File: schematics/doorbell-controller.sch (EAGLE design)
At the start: 2 parts

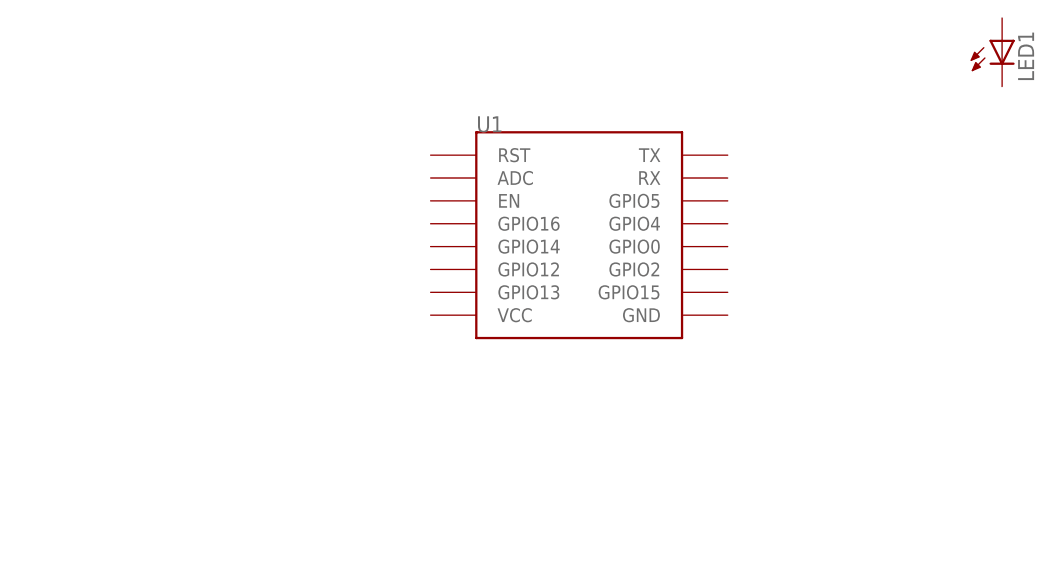
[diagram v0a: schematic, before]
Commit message: Added interrupt extender to schematics
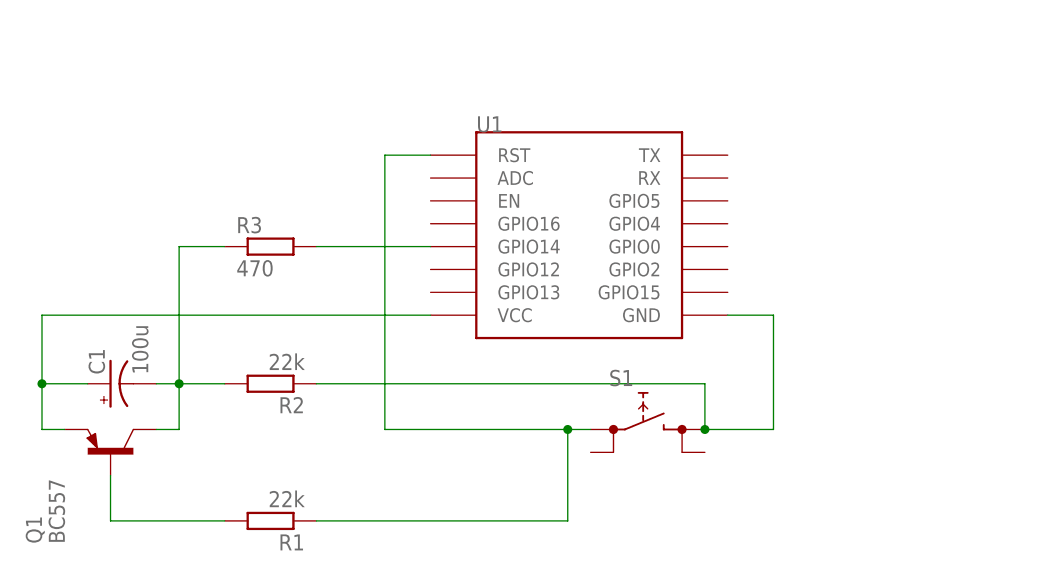
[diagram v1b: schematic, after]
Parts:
- removed LED1: (no value), led:LED5MM
- added C1: 100u, rcl:CPOL-USE2,5-6E
- added Q1: BC557, transistor-pnp:BC557
- added R1, R2: 22k, rcl:R-EU_0204/7
- added R3: 470, rcl:R-EU_0204/7
- added S1: (no value), switch:REKN
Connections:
- new net GND: R2.1, S1.1@A, U1.GND
- new net N$2: Q1.B, R1.2
- new net N$3: R3.2, U1.GPIO14
- new net N$5: C1.-, Q1.C, R2.2, R3.1
- new net N$8: C1.+, Q1.E, U1.VCC
- new net RST: R1.1, S1.0@A, U1.RST

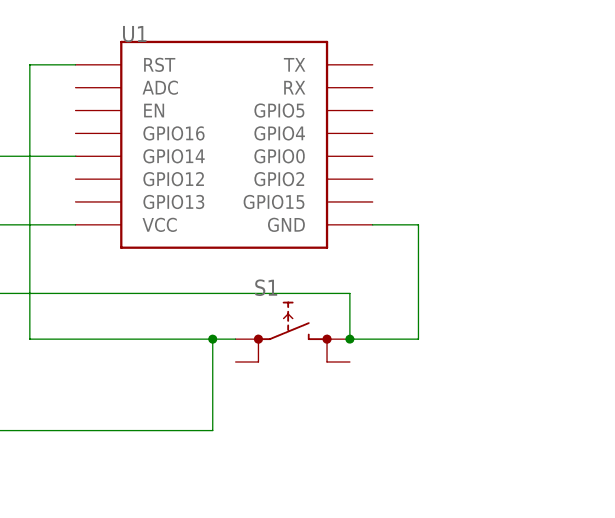
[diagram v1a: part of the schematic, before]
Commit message: Added LEDs to schematics; Replaces button with Clamp
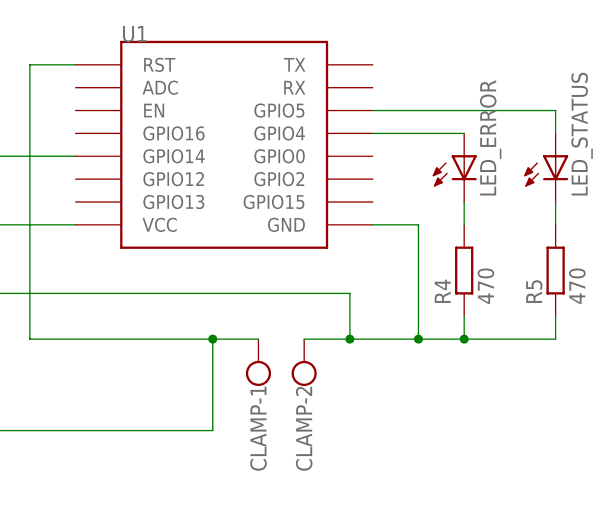
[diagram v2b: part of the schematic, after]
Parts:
- removed S1: (no value), switch:REKN
- added CLAMP: (no value), con-wago-500:W237-102
- added LED_ERROR, LED_STATUS: (no value), led:LED5MM
- added R4, R5: 470, rcl:R-EU_0204/7
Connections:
- new net N$1: LED_STATUS.A, U1.GPIO5
- new net N$4: LED_ERROR.A, U1.GPIO4
- new net N$6: LED_ERROR.C, R4.2
- new net N$7: LED_STATUS.C, R5.2
- net GND: now also CLAMP-2.KL, R4.1, R5.1; no longer S1.1@A
- net RST: now also CLAMP-1.KL; no longer S1.0@A
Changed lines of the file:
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@@
 <part name="R1" library="rcl" library_urn="urn:adsk.eagle:library:334" deviceset="R-EU_" device="0204/7" package3d_urn="urn:adsk.eagle:package:23498/1" value="22k"/>
 <part name="C1" library="rcl" library_urn="urn:adsk.eagle:library:334" deviceset="CPOL-US" device="E2,5-6E" package3d_urn="urn:adsk.eagle:package:23430/1" value="100u"/>
-<part name="S1" library="switch" library_urn="urn:adsk.eagle:library:380" deviceset="REKN" device="" package3d_urn="urn:adsk.eagle:package:27692/1"/>
 <part name="R2" library="rcl" library_urn="urn:adsk.eagle:library:334" deviceset="R-EU_" device="0204/7" package3d_urn="urn:adsk.eagle:package:23498/1" value="22k"/>
 <part name="Q1" library="transistor-pnp" library_urn="urn:adsk.eagle:library:399" deviceset="BC557" device="" package3d_urn="urn:adsk.eagle:package:29211/2"/>
 <part name="R3" library="rcl" library_urn="urn:adsk.eagle:library:334" deviceset="R-EU_" device="0204/7" package3d_urn="urn:adsk.eagle:package:23498/1" value="470"/>
+<part name="LED_STATUS" library="led" library_urn="urn:adsk.eagle:library:259" deviceset="LED" device="5MM" package3d_urn="urn:adsk.eagle:package:15799/2"/>
+<part name="LED_ERROR" library="led" library_urn="urn:adsk.eagle:library:259" deviceset="LED" device="5MM" package3d_urn="urn:adsk.eagle:package:15799/2"/>
+<part name="R4" library="rcl" library_urn="urn:adsk.eagle:library:334" deviceset="R-EU_" device="0204/7" package3d_urn="urn:adsk.eagle:package:23498/1" value="470"/>
+<part name="R5" library="rcl" library_urn="urn:adsk.eagle:library:334" deviceset="R-EU_" device="0204/7" package3d_urn="urn:adsk.eagle:package:23498/1" value="470"/>
+<part name="CLAMP" library="con-wago-500" library_urn="urn:adsk.eagle:library:195" deviceset="W237-102" device="" package3d_urn="urn:adsk.eagle:package:10688/1"/>
 </parts>
 <sheets>
@@
 <instance part="R1" gate="G$1" x="35.56" y="15.24" rot="R180"/>
 <instance part="C1" gate="G$1" x="17.78" y="30.48" rot="R90"/>
-<instance part="S1" gate="G$1" x="76.2" y="25.4"/>
 <instance part="R2" gate="G$1" x="35.56" y="30.48" rot="R180"/>
 <instance part="Q1" gate="G$1" x="17.78" y="22.86" rot="R90"/>
 <instance part="R3" gate="G$1" x="35.56" y="45.72"/>
+<instance part="LED_STATUS" gate="G$1" x="106.68" y="45.72"/>
+<instance part="LED_ERROR" gate="G$1" x="96.52" y="45.72"/>
+<instance part="R4" gate="G$1" x="96.52" y="33.02" rot="R90"/>
+<instance part="R5" gate="G$1" x="106.68" y="33.02" rot="R90"/>
+<instance part="CLAMP" gate="-1" x="73.66" y="20.32" rot="R90"/>
+<instance part="CLAMP" gate="-2" x="78.74" y="20.32" rot="R90"/>
 </instances>
 <busses>
@@
 <net name="GND" class="0">
 <segment>
-<pinref part="S1" gate="G$1" pin="1@A"/>
 <pinref part="R2" gate="G$1" pin="1"/>
 <wire x1="40.64" y1="30.48" x2="83.82" y2="30.48" width="0.1524" layer="91"/>
@@
 <wire x1="83.82" y1="25.4" x2="91.44" y2="25.4" width="0.1524" layer="91"/>
 <wire x1="91.44" y1="25.4" x2="91.44" y2="38.1" width="0.1524" layer="91"/>
+<pinref part="R4" gate="G$1" pin="1"/>
+<wire x1="96.52" y1="27.94" x2="96.52" y2="25.4" width="0.1524" layer="91"/>
+<wire x1="96.52" y1="25.4" x2="91.44" y2="25.4" width="0.1524" layer="91"/>
+<junction x="91.44" y="25.4"/>
+<pinref part="R5" gate="G$1" pin="1"/>
+<wire x1="106.68" y1="27.94" x2="106.68" y2="25.4" width="0.1524" layer="91"/>
+<wire x1="106.68" y1="25.4" x2="96.52" y2="25.4" width="0.1524" layer="91"/>
+<junction x="96.52" y="25.4"/>
+<pinref part="CLAMP" gate="-2" pin="KL"/>
+<wire x1="78.74" y1="25.4" x2="83.82" y2="25.4" width="0.1524" layer="91"/>
 <junction x="83.82" y="25.4"/>
 </segment>
@@
 <pinref part="U1" gate="G$1" pin="RST"/>
 <wire x1="48.26" y1="55.88" x2="53.34" y2="55.88" width="0.1524" layer="91"/>
-<pinref part="S1" gate="G$1" pin="0@A"/>
-<wire x1="71.12" y1="25.4" x2="68.58" y2="25.4" width="0.1524" layer="91"/>
 <wire x1="68.58" y1="25.4" x2="48.26" y2="25.4" width="0.1524" layer="91"/>
 <wire x1="48.26" y1="25.4" x2="48.26" y2="55.88" width="0.1524" layer="91"/>
 <wire x1="68.58" y1="15.24" x2="68.58" y2="25.4" width="0.1524" layer="91"/>
 <junction x="68.58" y="25.4"/>
+<pinref part="CLAMP" gate="-1" pin="KL"/>
+<wire x1="73.66" y1="25.4" x2="68.58" y2="25.4" width="0.1524" layer="91"/>
 </segment>
 </net>
@@
 </segment>
 </net>
+<net name="N$1" class="0">
+<segment>
+<pinref part="U1" gate="G$1" pin="GPIO5"/>
+<wire x1="86.36" y1="50.8" x2="106.68" y2="50.8" width="0.1524" layer="91"/>
+<pinref part="LED_STATUS" gate="G$1" pin="A"/>
+<wire x1="106.68" y1="50.8" x2="106.68" y2="48.26" width="0.1524" layer="91"/>
+</segment>
+</net>
+<net name="N$4" class="0">
+<segment>
+<pinref part="U1" gate="G$1" pin="GPIO4"/>
+<pinref part="LED_ERROR" gate="G$1" pin="A"/>
+<wire x1="86.36" y1="48.26" x2="96.52" y2="48.26" width="0.1524" layer="91"/>
+</segment>
+</net>
+<net name="N$6" class="0">
+<segment>
+<pinref part="LED_ERROR" gate="G$1" pin="C"/>
+<pinref part="R4" gate="G$1" pin="2"/>
+<wire x1="96.52" y1="40.64" x2="96.52" y2="38.1" width="0.1524" layer="91"/>
+</segment>
+</net>
+<net name="N$7" class="0">
+<segment>
+<pinref part="R5" gate="G$1" pin="2"/>
+<pinref part="LED_STATUS" gate="G$1" pin="C"/>
+<wire x1="106.68" y1="38.1" x2="106.68" y2="40.64" width="0.1524" layer="91"/>
+</segment>
+</net>

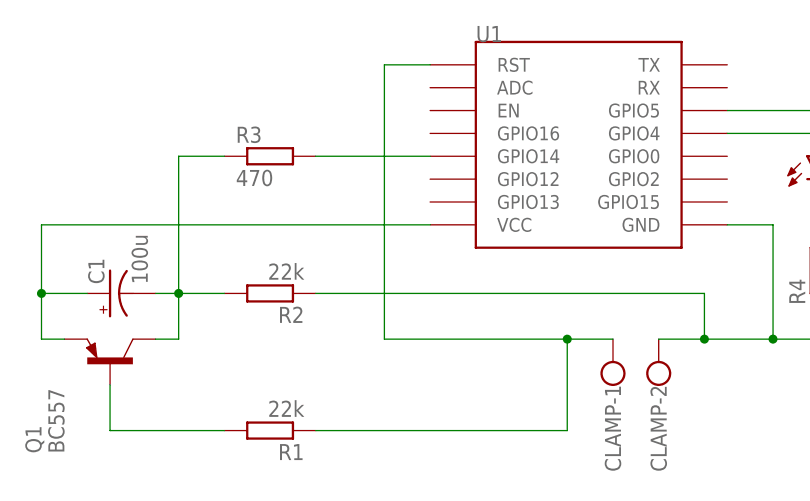
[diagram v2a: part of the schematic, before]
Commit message: Hooked up RST to GPIO16
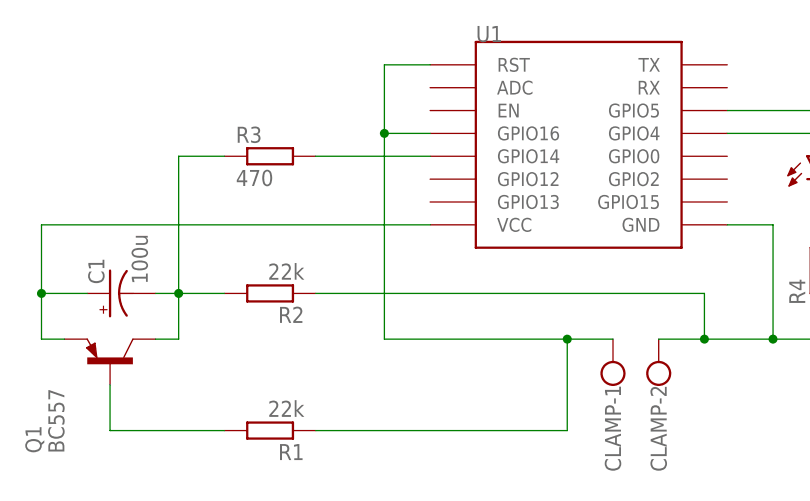
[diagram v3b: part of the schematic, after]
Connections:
- net RST: now also U1.GPIO16
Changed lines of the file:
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@@
 <wire x1="48.26" y1="55.88" x2="53.34" y2="55.88" width="0.1524" layer="91"/>
 <wire x1="68.58" y1="25.4" x2="48.26" y2="25.4" width="0.1524" layer="91"/>
-<wire x1="48.26" y1="25.4" x2="48.26" y2="55.88" width="0.1524" layer="91"/>
+<wire x1="48.26" y1="25.4" x2="48.26" y2="48.26" width="0.1524" layer="91"/>
+<wire x1="48.26" y1="48.26" x2="48.26" y2="55.88" width="0.1524" layer="91"/>
 <wire x1="68.58" y1="15.24" x2="68.58" y2="25.4" width="0.1524" layer="91"/>
 <junction x="68.58" y="25.4"/>
 <pinref part="CLAMP" gate="-1" pin="KL"/>
 <wire x1="73.66" y1="25.4" x2="68.58" y2="25.4" width="0.1524" layer="91"/>
+<pinref part="U1" gate="G$1" pin="GPIO16"/>
+<wire x1="53.34" y1="48.26" x2="48.26" y2="48.26" width="0.1524" layer="91"/>
+<junction x="48.26" y="48.26"/>
 </segment>
 </net>

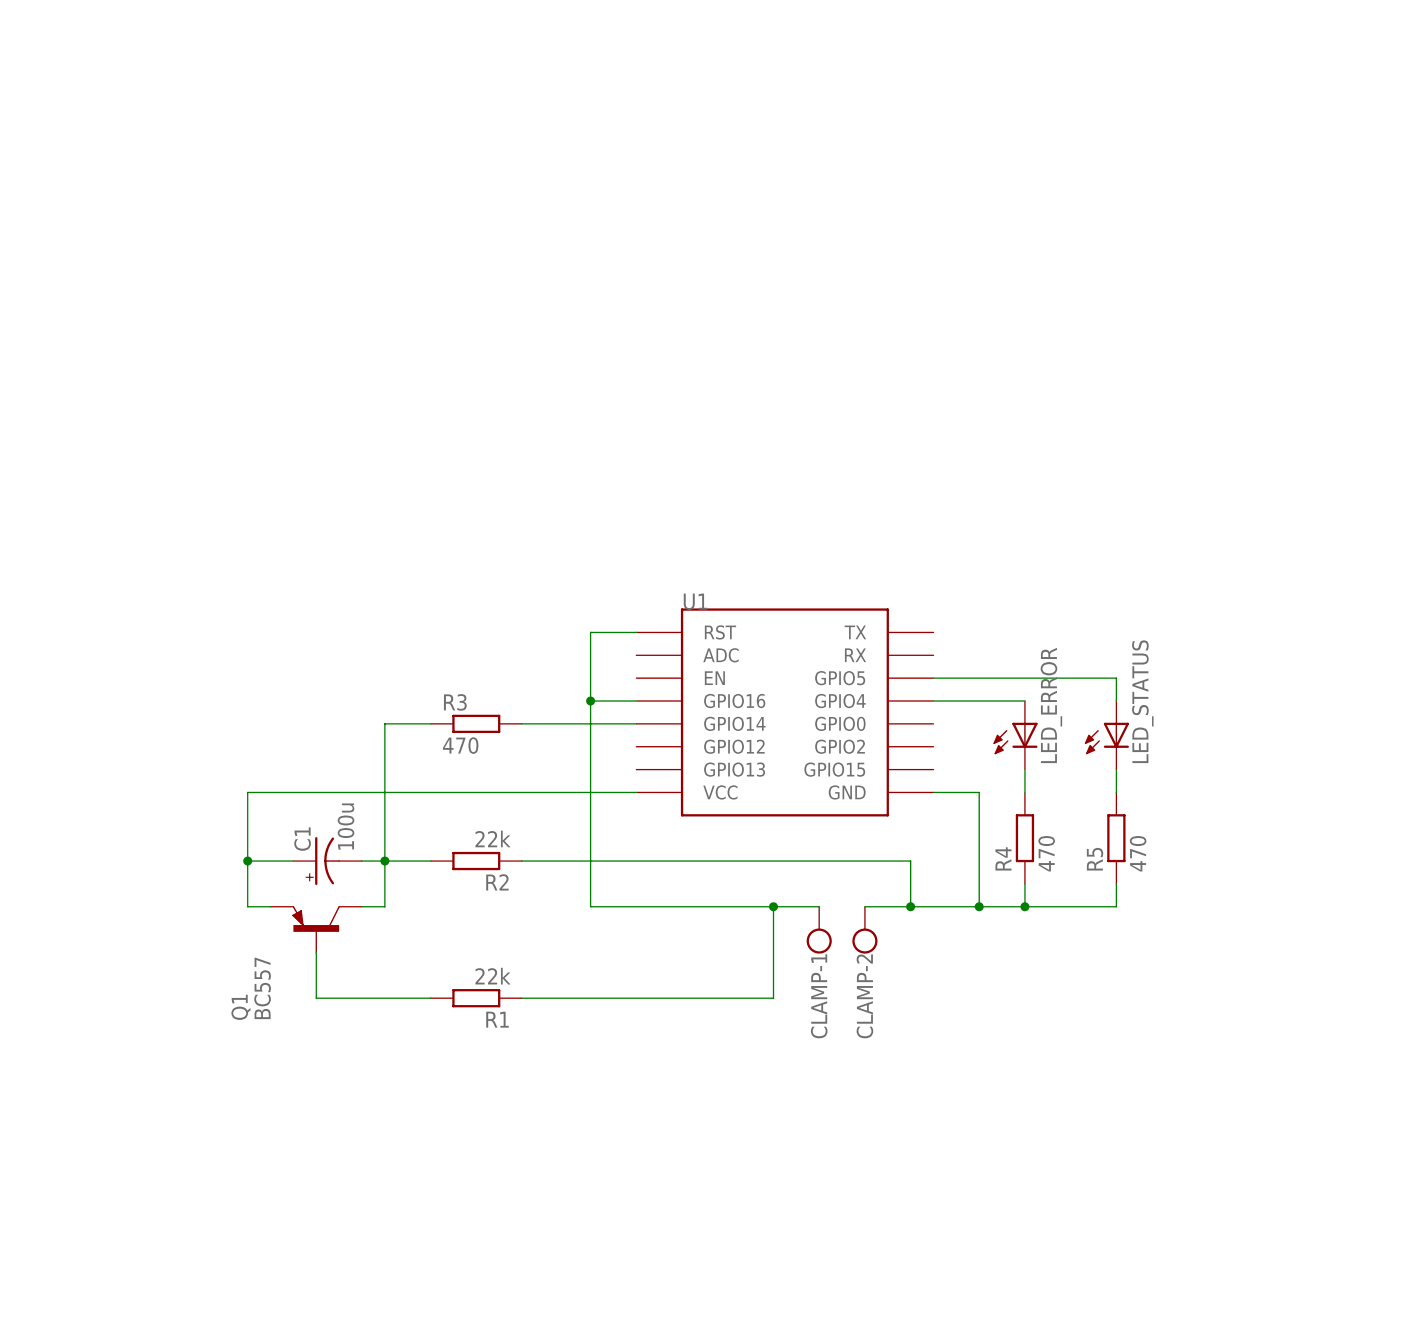
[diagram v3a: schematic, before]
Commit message: Updated Schematics to fit wall mount dimensions
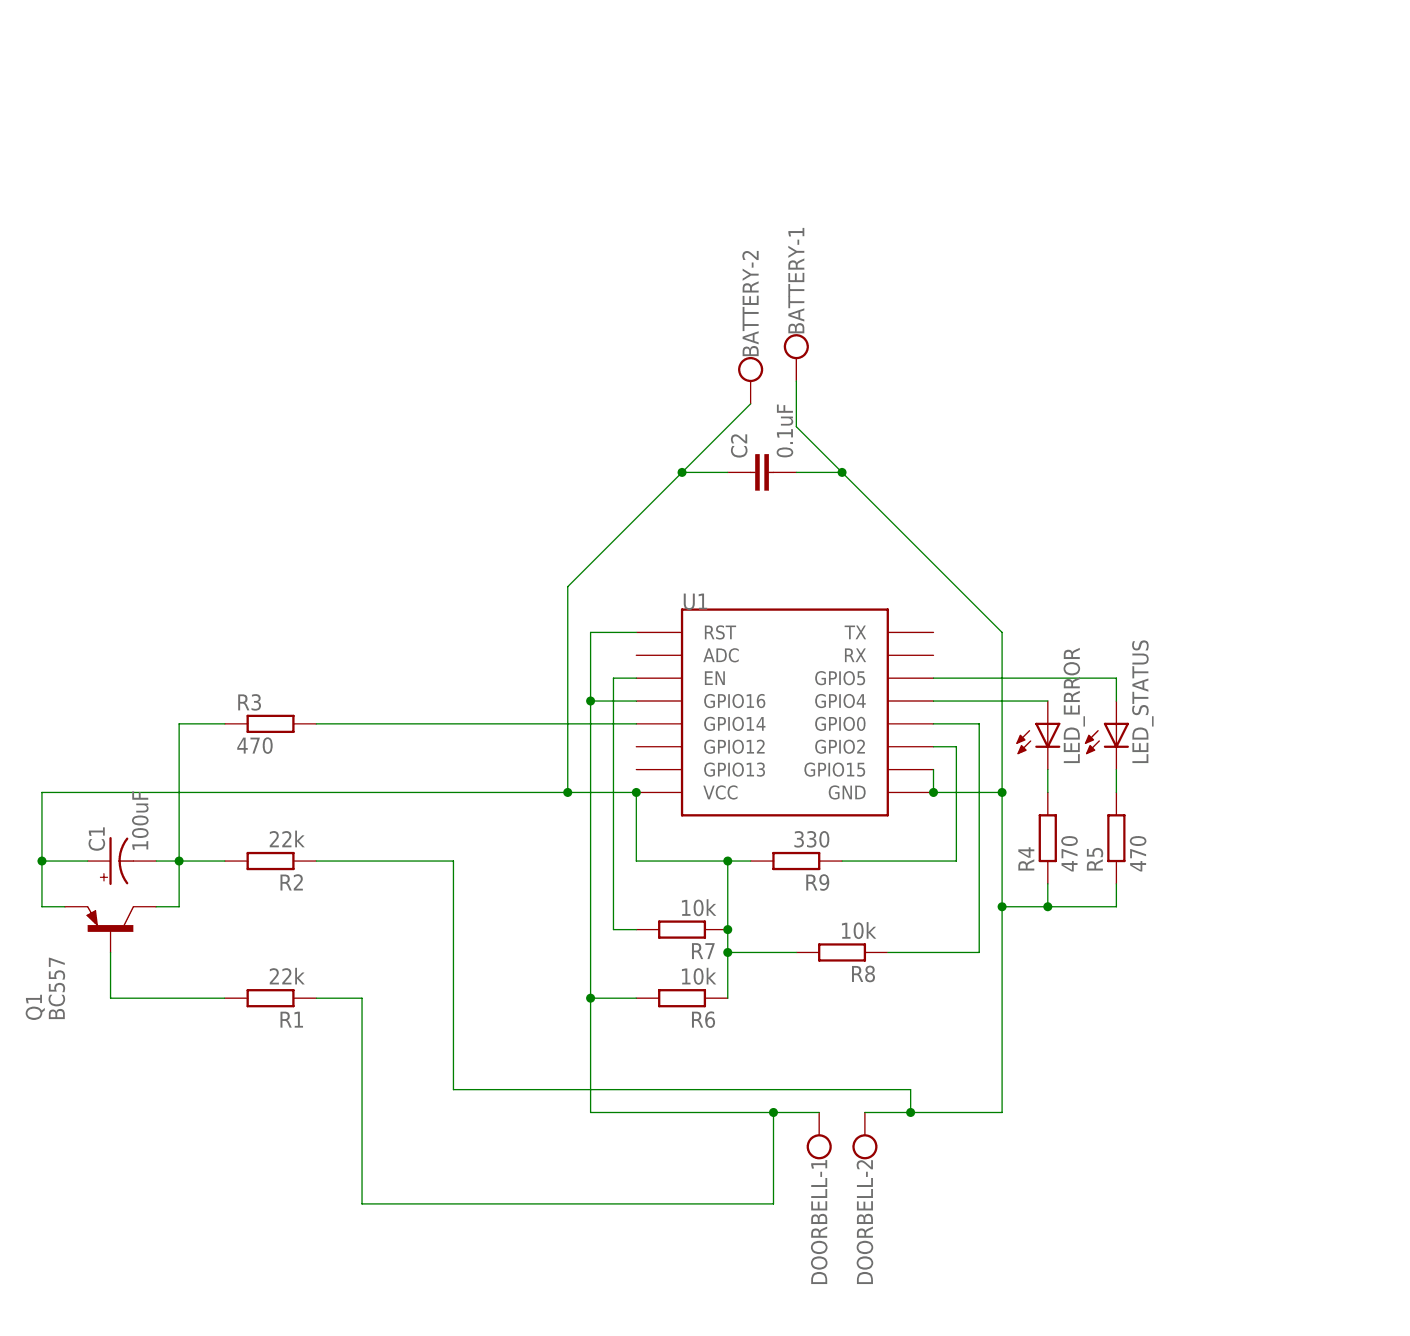
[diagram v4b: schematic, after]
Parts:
- removed CLAMP: (no value), con-wago-500:W237-102
- added BATTERY, DOORBELL: (no value), con-wago-500:W237-102
- added C2: 0.1uF, rcl:C-EU025-025X050
- added R6, R7, R8: 10k, rcl:R-EU_0204/7
- added R9: 330, rcl:R-EU_0204/7
- C1: value 100u -> 100uF
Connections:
- new net N$10: R7.2, U1.EN
- new net N$11: R8.1, U1.GPIO0
- new net N$9: R9.1, U1.GPIO2
- net GND: now also BATTERY-1.KL, C2.2, DOORBELL-2.KL, U1.GPIO15; no longer CLAMP-2.KL
- net N$8: now also BATTERY-2.KL, C2.1, R6.1, R7.1, R8.2, R9.2
- net RST: now also DOORBELL-1.KL, R6.2; no longer CLAMP-1.KL
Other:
- moved on the sheet: C1, LED_ERROR, Q1, R1, R2, R3, R4
